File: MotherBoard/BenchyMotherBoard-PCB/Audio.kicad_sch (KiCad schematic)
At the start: 3 parts, among them J2 LVDS-DISPLAY, U4 AM6254ATCGGAALW, U5 SiI9022ACNU

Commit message: (WIP) Finish more of the PS schematic
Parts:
- removed J2: LVDS-DISPLAY, symbol Daxxn_Displays:Generic-Display-LVDS
- removed U4: AM6254ATCGGAALW, Daxxn_Packages:ALW0425A-BGA-425-13x13mm, symbol Daxxn_TIMicros:AM6254ATCGGAALW
- removed U5: SiI9022ACNU, Package_DFN_QFN:QFN-72-1EP_10x10mm_P0.5mm_EP6x6mm, symbol Daxxn_IC:SiI9022ACNU
- added U4: AM6254ATCGGAALW, Daxxn_Packages:ALW0425A-BGA-425-13x13mm, symbol Daxxn_TIMicros:AM6254ATCGGAALW
- added U5: SiI9022ACNU, Package_DFN_QFN:QFN-72-1EP_10x10mm_P0.5mm_EP6x6mm, symbol Daxxn_IC:SiI9022ACNU

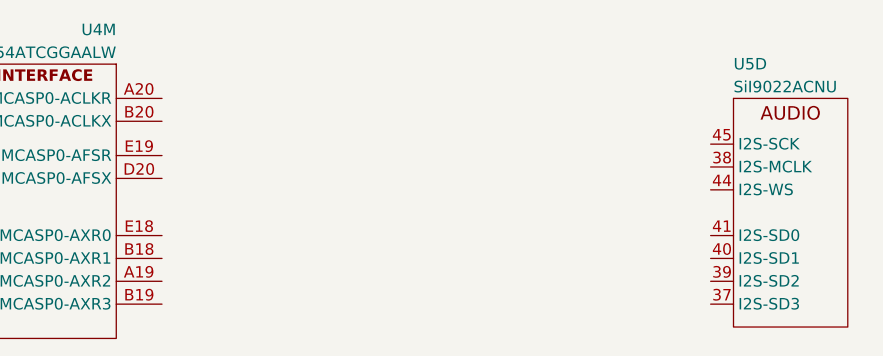
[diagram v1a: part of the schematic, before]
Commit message: (WIP) More work on power supply sequencing
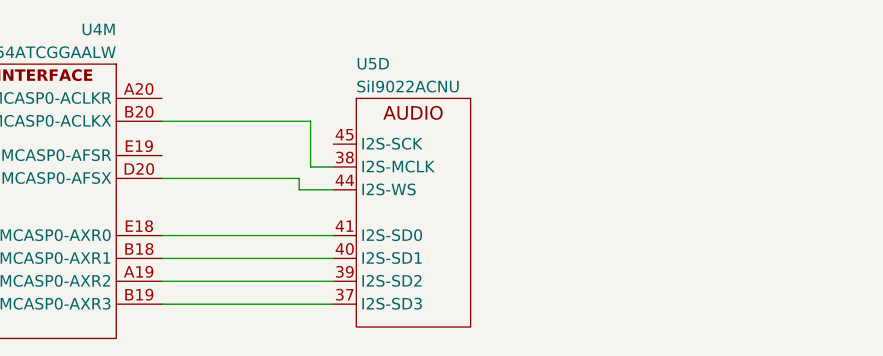
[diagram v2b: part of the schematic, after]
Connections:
- net at U5.37 (I2S-SD3): now also U4.B19 (MCASP0-AXR3)
- net at U5.38 (I2S-MCLK): now also U4.B20 (MCASP0-ACLKX)
- net at U5.39 (I2S-SD2): now also U4.A19 (MCASP0-AXR2)
- net at U5.40 (I2S-SD1): now also U4.B18 (MCASP0-AXR1)
- net at U5.41 (I2S-SD0): now also U4.E18 (MCASP0-AXR0)
- net at U5.44 (I2S-WS): now also U4.D20 (MCASP0-AFSX)
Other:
- moved on the sheet: U5D
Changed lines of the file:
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@@
     (company "Daxxn Industries")
   )
-  (symbol (lib_id "Daxxn_IC:SiI9022ACNU") (at 133.35 43.18 0) (unit 4)
+  (wire (pts (xy 88.9 66.04) (xy 69.85 66.04))
+    (stroke (width 0) (type default))
+  )
+  (wire (pts (xy 88.9 58.42) (xy 69.85 58.42))
+    (stroke (width 0) (type default))
+  )
+  (wire (pts (xy 88.9 50.8) (xy 86.36 50.8))
+    (stroke (width 0) (type default))
+  )
+  (wire (pts (xy 85.09 53.34) (xy 88.9 53.34))
+    (stroke (width 0) (type default))
+  )
+  (wire (pts (xy 69.85 52.07) (xy 85.09 52.07))
+    (stroke (width 0) (type default))
+  )
+  (wire (pts (xy 88.9 63.5) (xy 69.85 63.5))
+    (stroke (width 0) (type default))
+  )
+  (wire (pts (xy 88.9 60.96) (xy 69.85 60.96))
+    (stroke (width 0) (type default))
+  )
+  (wire (pts (xy 69.85 45.72) (xy 86.36 45.72))
+    (stroke (width 0) (type default))
+  )
+  (wire (pts (xy 85.09 52.07) (xy 85.09 53.34))
+    (stroke (width 0) (type default))
+  )
+  (wire (pts (xy 86.36 45.72) (xy 86.36 50.8))
+    (stroke (width 0) (type default))
+  )
+  (symbol (lib_id "Daxxn_IC:SiI9022ACNU") (at 91.44 43.18 0) (unit 4)
     (in_bom yes) (on_board yes) (dnp no)
-    (property "Reference" "U5" (at 133.35 39.37 0)
+    (property "Reference" "U5" (at 91.44 39.37 0)
       (effects (font (size 1.27 1.27)) (justify left))
     )
-    (property "Value" "SiI9022ACNU" (at 133.35 41.91 0)
+    (property "Value" "SiI9022ACNU" (at 91.44 41.91 0)
       (effects (font (size 1.27 1.27)) (justify left))
     )
-    (property "Footprint" "Package_DFN_QFN:QFN-72-1EP_10x10mm_P0.5mm_EP6x6mm" (at 146.05 31.75 0)
+    (property "Footprint" "Package_DFN_QFN:QFN-72-1EP_10x10mm_P0.5mm_EP6x6mm" (at 104.14 31.75 0)
       (effects (font (size 1.27 1.27)) hide)
     )
-    (property "Datasheet" "%LOCAL_DATASHEETS%/SIL9022.pdf" (at 146.05 34.29 0)
+    (property "Datasheet" "%LOCAL_DATASHEETS%/SIL9022.pdf" (at 104.14 34.29 0)
       (effects (font (size 1.27 1.27)) hide)
     )

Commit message: Start PCB layout
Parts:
- U5: footprint Package_DFN_QFN:QFN-72-1EP_10x10mm_P0.5mm_EP6x6mm -> Daxxn_Packages:QFN-72-1EP_10x10mm_P0.5mm_EP6x6mm
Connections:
- net at U5.37 (I2S-SD3): no longer U4.B19 (MCASP0-AXR3)
- net at U5.38 (I2S-MCLK): no longer U4.B20 (MCASP0-ACLKX)
- net at U5.39 (I2S-SD2): no longer U4.A19 (MCASP0-AXR2)
- net at U5.40 (I2S-SD1): no longer U4.B18 (MCASP0-AXR1)
- net at U5.41 (I2S-SD0): no longer U4.E18 (MCASP0-AXR0)
- net at U5.44 (I2S-WS): no longer U4.D20 (MCASP0-AFSX)
- no-connect marks 0 -> 15
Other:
- note added: "NO AUDIO REQUIRED"
- moved on the sheet: U4M, U5D
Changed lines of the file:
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@@
 (kicad_sch (version 20230121) (generator eeschema)
-  (paper "A4")
+  (paper "User" 150.012 99.9998)
   (title_block
     (title "Benchy Reloaded")
@@
     (company "Daxxn Industries")
   )
-  (wire (pts (xy 88.9 66.04) (xy 69.85 66.04))
-    (stroke (width 0) (type default))
+  (no_connect (at 43.18 43.18))
+  (no_connect (at 43.18 34.29))
+  (no_connect (at 62.23 35.56))
+  (no_connect (at 62.23 38.1))
+  (no_connect (at 62.23 50.8))
+  (no_connect (at 43.18 27.94))
+  (no_connect (at 62.23 45.72))
+  (no_connect (at 43.18 30.48))
+  (no_connect (at 43.18 50.8))
+  (no_connect (at 62.23 33.02))
+  (no_connect (at 62.23 48.26))
+  (no_connect (at 62.23 43.18))
+  (no_connect (at 43.18 45.72))
+  (no_connect (at 43.18 48.26))
+  (no_connect (at 43.18 36.83))
+  (text "NO AUDIO REQUIRED" (at 15.24 16.51 0)
+    (effects (font (size 2 2) (thickness 0.4) bold) (justify left bottom))
   )
-  (wire (pts (xy 88.9 58.42) (xy 69.85 58.42))
-    (stroke (width 0) (type default))
-  )
-  (wire (pts (xy 88.9 50.8) (xy 86.36 50.8))
-    (stroke (width 0) (type default))
-  )
-  (wire (pts (xy 85.09 53.34) (xy 88.9 53.34))
-    (stroke (width 0) (type default))
-  )
-  (wire (pts (xy 69.85 52.07) (xy 85.09 52.07))
-    (stroke (width 0) (type default))
-  )
-  (wire (pts (xy 88.9 63.5) (xy 69.85 63.5))
-    (stroke (width 0) (type default))
-  )
-  (wire (pts (xy 88.9 60.96) (xy 69.85 60.96))
-    (stroke (width 0) (type default))
-  )
-  (wire (pts (xy 69.85 45.72) (xy 86.36 45.72))
-    (stroke (width 0) (type default))
-  )
-  (wire (pts (xy 85.09 52.07) (xy 85.09 53.34))
-    (stroke (width 0) (type default))
-  )
-  (wire (pts (xy 86.36 45.72) (xy 86.36 50.8))
-    (stroke (width 0) (type default))
-  )
-  (symbol (lib_id "Daxxn_IC:SiI9022ACNU") (at 91.44 43.18 0) (unit 4)
+  (symbol (lib_id "Daxxn_IC:SiI9022ACNU") (at 64.77 27.94 0) (unit 4)
     (in_bom yes) (on_board yes) (dnp no)
-    (property "Reference" "U5" (at 91.44 39.37 0)
+    (property "Reference" "U5" (at 64.77 24.13 0)
       (effects (font (size 1.27 1.27)) (justify left))
     )
-    (property "Value" "SiI9022ACNU" (at 91.44 41.91 0)
+    (property "Value" "SiI9022ACNU" (at 64.77 26.67 0)
       (effects (font (size 1.27 1.27)) (justify left))
     )
-    (property "Footprint" "Package_DFN_QFN:QFN-72-1EP_10x10mm_P0.5mm_EP6x6mm" (at 104.14 31.75 0)
-      (effects (font (size 1.27 1.27)) hide)
-    )
-    (property "Datasheet" "%LOCAL_DATASHEETS%/SIL9022.pdf" (at 104.14 34.29 0)
+    (property "Footprint" "Daxxn_Packages:QFN-72-1EP_10x10mm_P0.5mm_EP6x6mm" (at 77.47 16.51 0)
+      (effects (font (size 1.27 1.27)) hide)
+    )
+    (property "Datasheet" "%LOCAL_DATASHEETS%/SIL9022.pdf" (at 77.47 19.05 0)
+      (effects (font (size 1.27 1.27)) hide)
+    )
+    (property "Schematic" "" (at 64.77 27.94 0)
+      (effects (font (size 1.27 1.27)) hide)
+    )
+    (property "PartNumber" "" (at 64.77 27.94 0)
+      (effects (font (size 1.27 1.27)))
+    )
+    (property "SupplierPN" "" (at 64.77 27.94 0)
       (effects (font (size 1.27 1.27)) hide)
     )
@@
     )
   )
-  (symbol (lib_id "Daxxn_TIMicros:AM6254ATCGGAALW") (at 64.77 39.37 0) (mirror y) (unit 13)
+  (symbol (lib_id "Daxxn_TIMicros:AM6254ATCGGAALW") (at 38.1 24.13 0) (mirror y) (unit 13)
     (in_bom yes) (on_board yes) (dnp no)
-    (property "Reference" "U4" (at 64.77 35.56 0)
+    (property "Reference" "U4" (at 38.1 20.32 0)
       (effects (font (size 1.27 1.27)) (justify left))
     )
-    (property "Value" "AM6254ATCGGAALW" (at 64.77 38.1 0)
+    (property "Value" "AM6254ATCGGAALW" (at 38.1 22.86 0)
       (effects (font (size 1.27 1.27)) (justify left))
     )
-    (property "Footprint" "Daxxn_Packages:ALW0425A-BGA-425-13x13mm" (at 46.99 31.75 0)
-      (effects (font (size 1.27 1.27)) hide)
-    )
-    (property "Datasheet" "%LOCAL_DATASHEETS%/AM625.pdf" (at 45.72 34.29 0)
-      (effects (font (size 1.27 1.27)) hide)
-    )
-    (property "Schematic" "" (at 64.77 39.37 0)
-      (effects (font (size 1.27 1.27)) hide)
-    )
-    (property "PartNumber" "" (at 64.77 39.37 0)
+    (property "Footprint" "Daxxn_Packages:ALW0425A-BGA-425-13x13mm" (at 20.32 16.51 0)
+      (effects (font (size 1.27 1.27)) hide)
+    )
+    (property "Datasheet" "%LOCAL_DATASHEETS%/AM625.pdf" (at 19.05 19.05 0)
+      (effects (font (size 1.27 1.27)) hide)
+    )
+    (property "Schematic" "" (at 38.1 24.13 0)
+      (effects (font (size 1.27 1.27)) hide)
+    )
+    (property "PartNumber" "" (at 38.1 24.13 0)
       (effects (font (size 1.27 1.27)))
     )
-    (property "SupplierPN" "" (at 64.77 39.37 0)
+    (property "SupplierPN" "" (at 38.1 24.13 0)
       (effects (font (size 1.27 1.27)) hide)
     )
@@
     (pin "E14")
     (pin "E15")
-    (pin "K22")
-    (pin "K24")
+    (pin "K22" (alternate "GPIO0-43"))
+    (pin "K24" (alternate "GPIO0-44"))
     (pin "K25")
-    (pin "L21")
+    (pin "L21" (alternate "GPIO0-42"))
     (pin "L23")
     (pin "L24")
     (pin "L25")
-    (pin "M21")
+    (pin "M21" (alternate "GPIO0-41"))
     (pin "M22")
-    (pin "M24")
-    (pin "M25" (alternate "TRC-CLK"))
+    (pin "M24" (alternate "GPIO0-35"))
+    (pin "M25" (alternate "GPIO0-15"))
     (pin "N20")
-    (pin "N23" (alternate "TRC-CTL"))
-    (pin "N24" (alternate "TRC-DATA0"))
-    (pin "N25" (alternate "TRC-DATA1"))
-    (pin "P21" (alternate "TRC-DATA4"))
-    (pin "P22" (alternate "TRC-DATA3"))
-    (pin "P24" (alternate "TRC-DATA2"))
+    (pin "N23" (alternate "GPIO0-16"))
+    (pin "N24" (alternate "GPIO0-17"))
+    (pin "N25" (alternate "GPIO0-18"))
+    (pin "P21" (alternate "GPIO0-21"))
+    (pin "P22" (alternate "GPIO0-20"))
+    (pin "P24" (alternate "GPIO0-19"))
     (pin "P25")
-    (pin "R21")
-    (pin "R23" (alternate "TRC-DATA5"))
-    (pin "R24")
-    (pin "R25")
-    (pin "T22")
-    (pin "T24")
-    (pin "T25")
-    (pin "U23")
-    (pin "U24")
-    (pin "U25")
-    (pin "V25")
+    (pin "R21" (alternate "VOUT0-DATA19"))
+    (pin "R23" (alternate "GPIO0-22"))
+    (pin "R24" (alternate "VOUT0-DATA16"))
+    (pin "R25" (alternate "VOUT0-DATA17"))
+    (pin "T22" (alternate "VOUT0-DATA20"))
+    (pin "T24" (alternate "VOUT0-DATA21"))
+    (pin "T25" (alternate "VOUT0-DATA18"))
+    (pin "U23" (alternate "GPIO0-37"))
+    (pin "U24" (alternate "VOUT0-DATA23"))
+    (pin "U25" (alternate "VOUT0-DATA22"))
+    (pin "V25" (alternate "GPIO0-38"))
     (pin "A21")
     (pin "A22")
@@
         )
         (path "/2ea077fe-b0e6-467f-a1c1-8336ebdb7a86/31cd65d1-cc4b-4775-aec3-7a59b690ac0a"
-          (reference "U4") (unit 13)
+          (reference "U1") (unit 13)
         )
       )

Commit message: Replacing motherboard and more - SAVE
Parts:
- renumbered U4 to U1
